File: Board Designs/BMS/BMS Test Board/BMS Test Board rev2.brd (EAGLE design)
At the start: 38.5 x 47.9 mm, 35 parts, among them IC1 OKI-78SR-5, IC2 NE5532SOIC

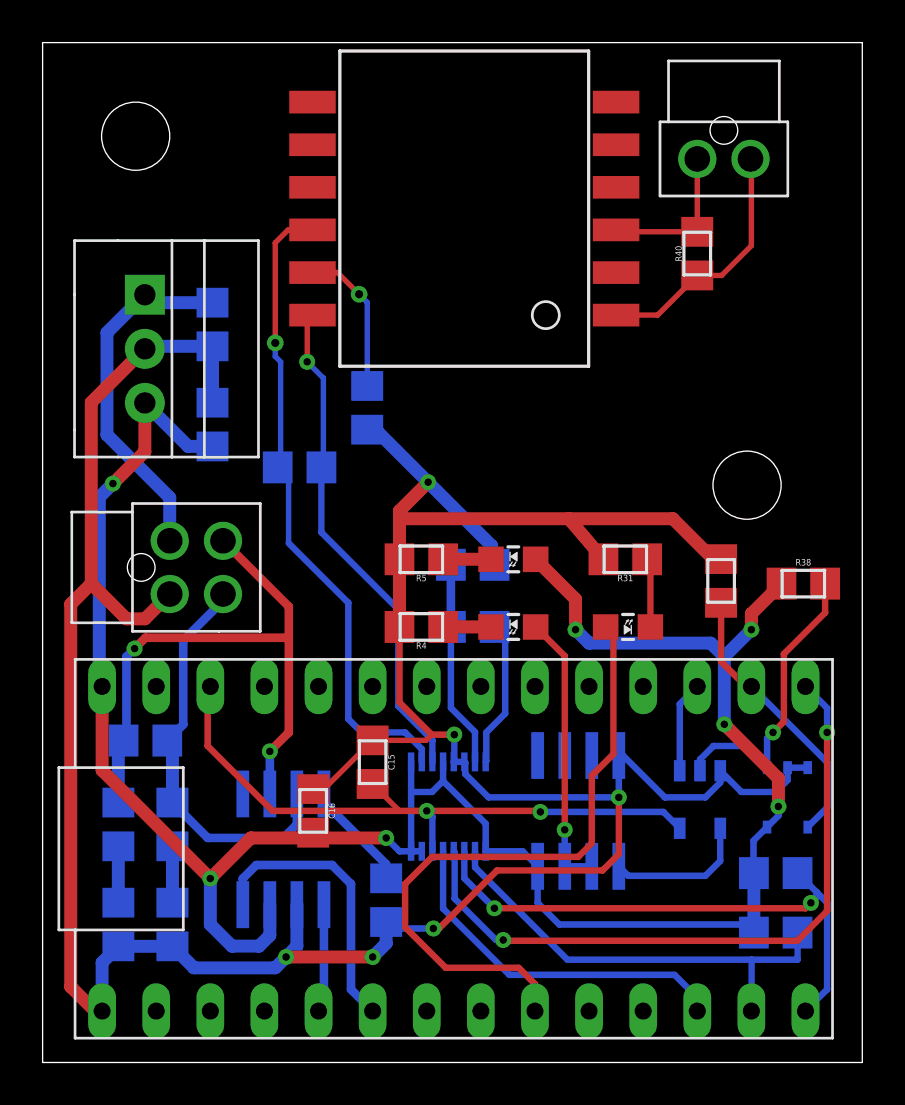
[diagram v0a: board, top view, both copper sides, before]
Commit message: Tweaked BMS test board, added rev2 with swapped SPI mode resistors
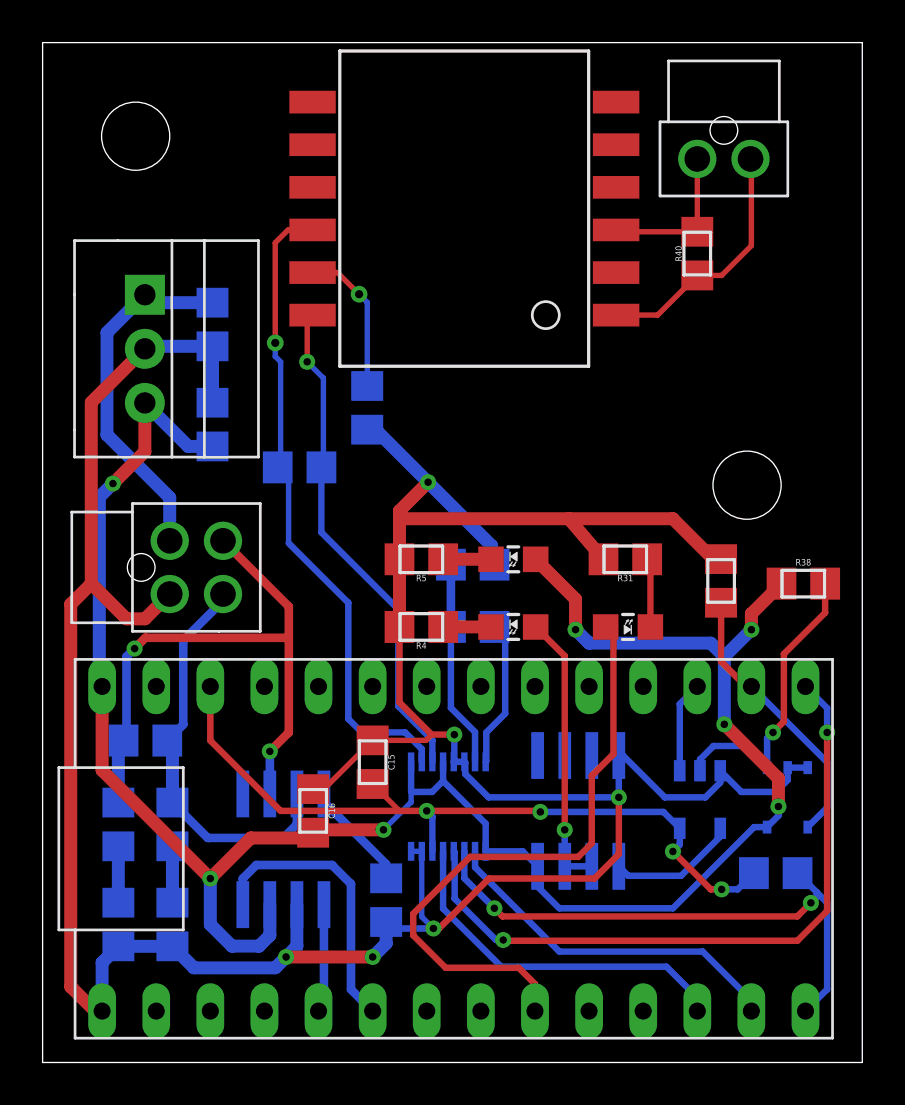
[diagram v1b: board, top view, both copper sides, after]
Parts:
- removed R36: 2k, HyTechDevices:0805
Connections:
- net +3V3: now also R37.1
- net +5V: no longer R36.1, R37.1, U$8.7, U$8.8
- net GND: now also U$8.7, U$8.8
- net MOSI_TEENSY: no longer R36.2
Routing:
- net +5V: track 104.4 -> 98.0 mm
- net +3V3: track 31.7 -> 37.4 mm, vias 2 -> 4
- net MOSI_TEENSY: track 21.4 -> 16.8 mm
- net GND: track 151.7 -> 156.0 mm
- net N$37: track 30.8 -> 29.5 mm
- net BMS_OK: track 6.77 -> 6.10 mm
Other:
- board text added: "2019 BMS Test board rev2"
- board text removed: "2019 BMS Test board rev1"
